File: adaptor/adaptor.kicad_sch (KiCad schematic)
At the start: 2 parts, among them CN1 XT30(2+2)PB-M.G.B, CN2 XT30(2+2)PB-M.G.B

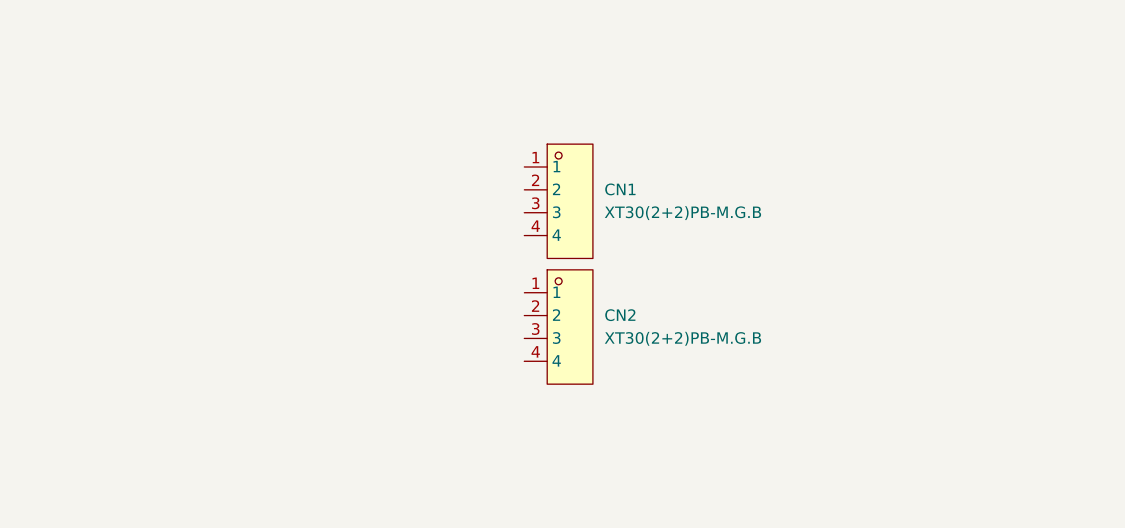
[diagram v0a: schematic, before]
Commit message: [Hw] Rough adaptor board layout, and form factor
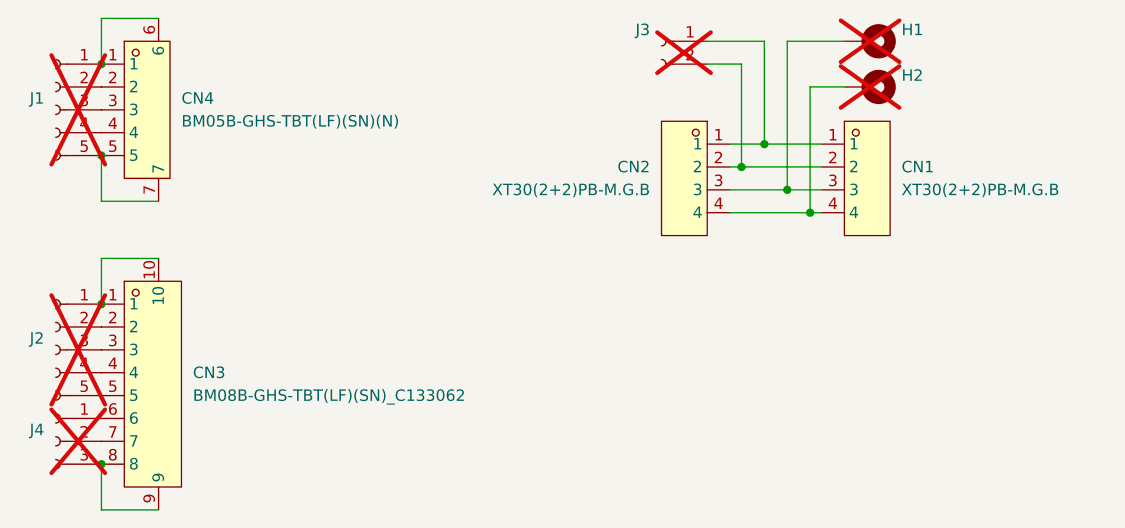
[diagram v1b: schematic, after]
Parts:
- added CN3: BM08B-GHS-TBT(LF)(SN)_C133062, easyeda:CONN-SMD_BM08B-GHS-TBT-LF-SN, symbol easyeda:BM08B-GHS-TBT(LF)(SN)_C133062
- added CN4: BM05B-GHS-TBT(LF)(SN)(N), easyeda:CONN-SMD_BM05B-GHS-TBT, symbol easyeda:BM05B-GHS-TBT(LF)(SN)(N)
- added H1, H2: ~, TestPoint:TestPoint_Keystone_5005-5009_Compact, symbol Mechanical:MountingHole_Pad
- added J1, J2: Conn_01x05_Socket, Connector_PinHeader_2.00mm:PinHeader_1x05_P2.00mm_Vertical, symbol Connector:Conn_01x05_Socket
- added J3: ~, Connector_PinHeader_2.00mm:PinHeader_1x02_P2.00mm_Vertical, symbol Connector:Conn_01x02_Socket
- added J4: Conn_01x05_Socket, Connector_PinHeader_2.00mm:PinHeader_1x03_P2.00mm_Vertical, symbol Connector:Conn_01x03_Socket
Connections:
- net at CN1.1: now also CN2.1, J3.1 (Pin_1)
- net at CN1.2: now also CN2.2, J3.2 (Pin_2)
- net at CN1.3: now also CN2.3, H1.1
- net at CN1.4: now also CN2.4, H2.1
- new net: CN3.1, CN3.10, J2.1 (Pin_1)
- new net: CN3.2, J2.2 (Pin_2)
- new net: CN3.3, J2.3 (Pin_3)
- new net: CN3.4, J2.4 (Pin_4)
- new net: CN3.5, J2.5 (Pin_5)
- new net: CN4.1, CN4.6, J1.1 (Pin_1)
- new net: CN4.2, J1.2 (Pin_2)
- new net: CN4.3, J1.3 (Pin_3)
- new net: CN4.4, J1.4 (Pin_4)
- new net: CN4.5, CN4.7, J1.5 (Pin_5)
- new net: CN3.6, J4.1 (Pin_1)
- new net: CN3.7, J4.2 (Pin_2)
- new net: CN3.8, CN3.9, J4.3 (Pin_3)
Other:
- moved on the sheet: CN1, CN2

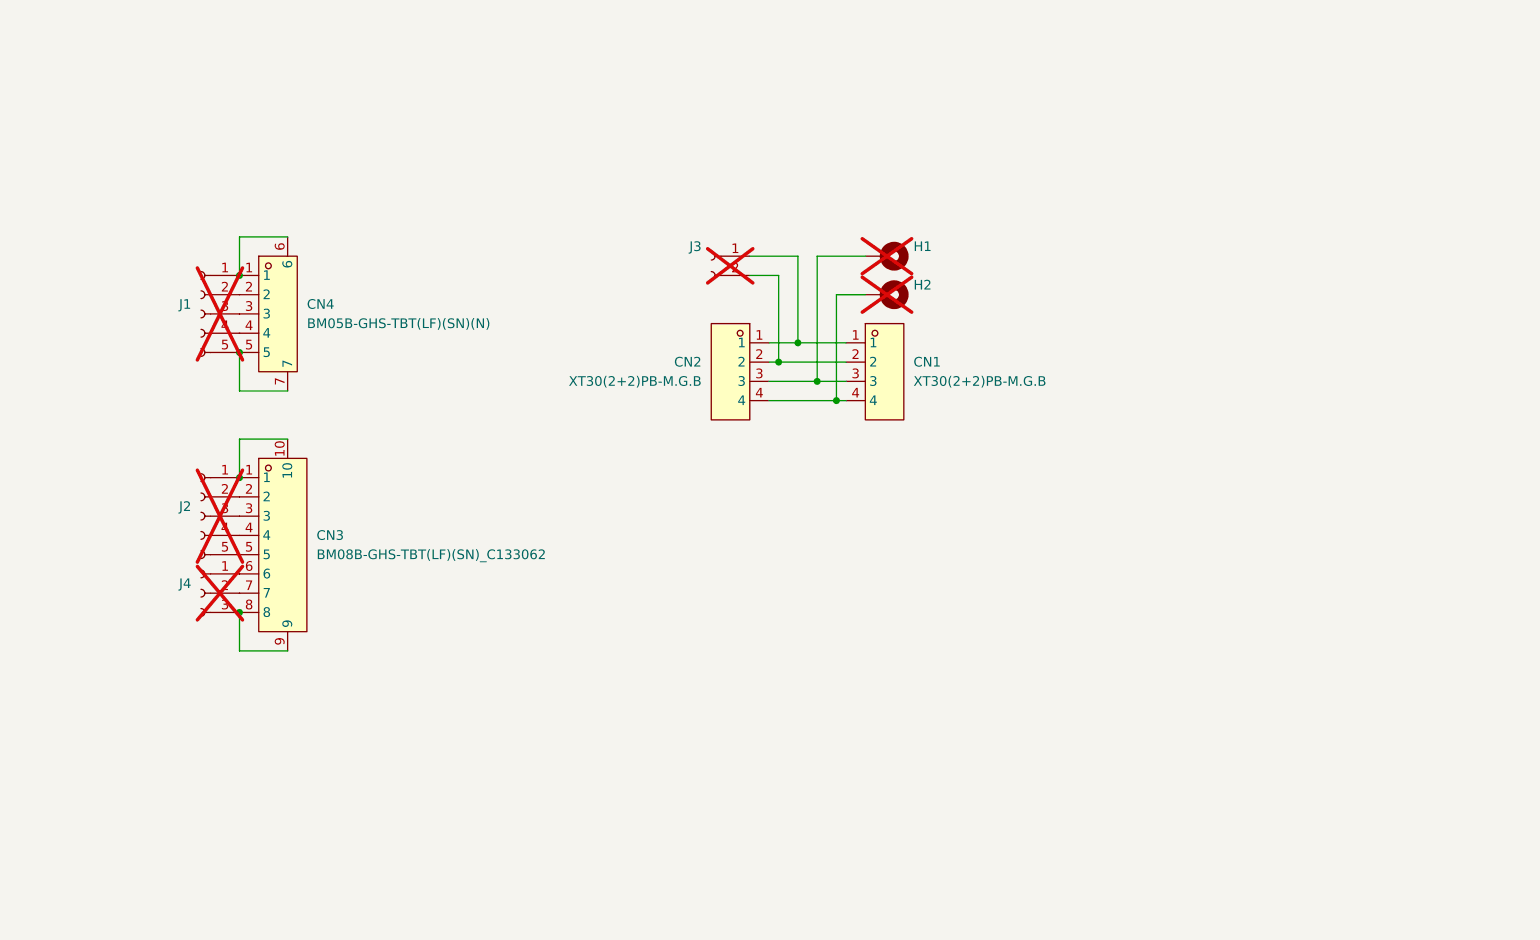
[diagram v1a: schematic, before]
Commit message: Adaptor boards
- CAN/Power XT30 2+2
- Break out Aux ports to 10 and 8 pin jst GH
- AS5046D encoder board with 10 pin jst GH connector

Signed-off-by: Will Haarhoff <williamhaarhoff@gmail.com>
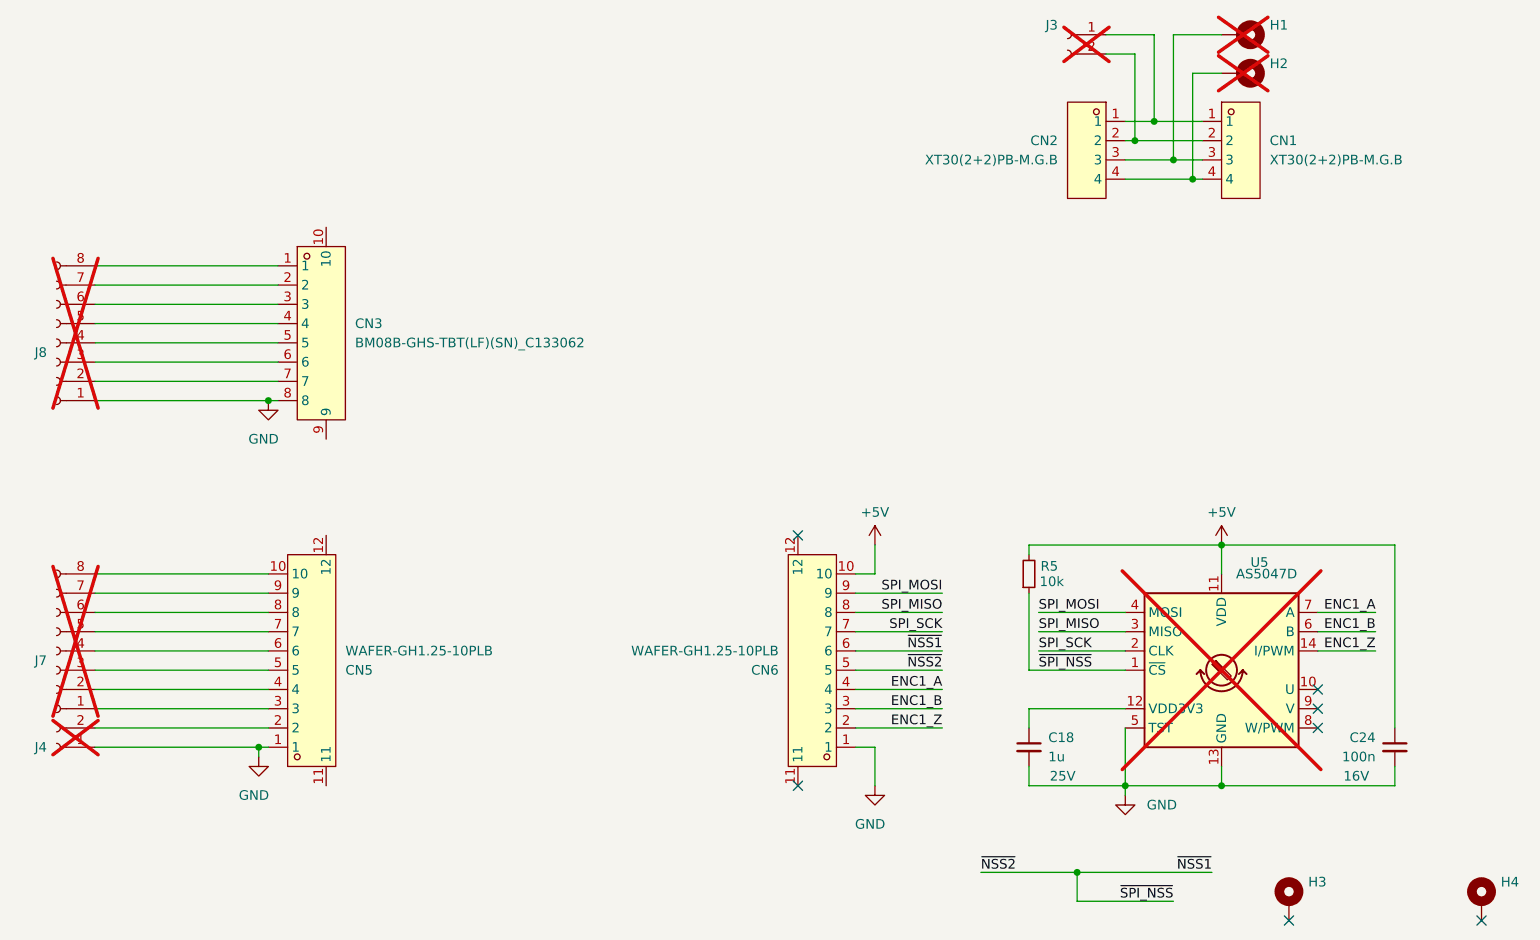
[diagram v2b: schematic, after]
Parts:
- removed CN4: BM05B-GHS-TBT(LF)(SN)(N), easyeda:CONN-SMD_BM05B-GHS-TBT, symbol easyeda:BM05B-GHS-TBT(LF)(SN)(N)
- removed J1, J2: Conn_01x05_Socket, Connector_PinHeader_2.00mm:PinHeader_1x05_P2.00mm_Vertical, symbol Connector:Conn_01x05_Socket
- removed J4: Conn_01x05_Socket, Connector_PinHeader_2.00mm:PinHeader_1x03_P2.00mm_Vertical, symbol Connector:Conn_01x03_Socket
- added C18: 1u, Capacitor_SMD:C_0402_1005Metric, symbol Device:C_Small
- added C24: 100n, Capacitor_SMD:C_0402_1005Metric, symbol Device:C_Small
- added CN5, CN6: WAFER-GH1.25-10PLB, easyeda:CONN-SMD_10P-P1.25_XUNPU_WAFER-GH1.25-10PLB, symbol easyeda:WAFER-GH1.25-10PLB
- added H3, H4: MountingHole_Pad, MountingHole:MountingHole_3.2mm_M3_ISO7380_Pad_TopBottom, symbol Mechanical:MountingHole_Pad
- added J4: Conn_01x02_Socket, Connector_PinHeader_1.27mm:PinHeader_1x02_P1.27mm_Vertical, symbol Connector:Conn_01x02_Socket
- added J7, J8: Conn_01x08_Socket, Connector_PinHeader_1.27mm:PinHeader_1x08_P1.27mm_Vertical, symbol Connector:Conn_01x08_Socket
- added R5: 10k, Resistor_SMD:R_0402_1005Metric, symbol Device:R_Small
- added U5: AS5047D, Package_SO:TSSOP-14_4.4x5mm_P0.65mm, symbol Sensor_Magnetic:AS5047D
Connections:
- net at CN3.1: now also J8.8 (Pin_8); no longer CN3.10
- net at CN3.2: now also J8.7 (Pin_7)
- net at CN3.3: now also J8.6 (Pin_6)
- net at CN3.4: now also J8.5 (Pin_5)
- net at CN3.5: now also J8.4 (Pin_4)
- net at CN3.6: now also J8.3 (Pin_3)
- net at CN3.7: now also J8.2 (Pin_2)
- net at CN3.9: no longer CN3.8
- new net: C18.1, U5.12 (VDD3V3)
- new net: CN5.3, J7.1 (Pin_1)
- new net: CN5.4, J7.2 (Pin_2)
- new net: CN5.5, J7.3 (Pin_3)
- new net: CN5.6, J7.4 (Pin_4)
- new net: CN5.7, J7.5 (Pin_5)
- new net: CN5.8, J7.6 (Pin_6)
- new net: CN5.9, J7.7 (Pin_7)
- new net: CN5.10, J7.8 (Pin_8)
- new net: CN5.2, J4.2 (Pin_2)
- new net +5V: C24.1, CN6.10, R5.2, U5.11 (VDD)
- new net ENC1_A: CN6.4, U5.7 (A)
- new net ENC1_B: CN6.3, U5.6 (B)
- new net ENC1_Z: CN6.2, U5.14 (I/PWM)
- new net GND: C18.2, C24.2, CN3.8, CN5.1, CN6.1, J4.1 (Pin_1), J8.1 (Pin_1), U5.13 (GND), U5.5 (TST)
- new net SPI_MISO: CN6.8, U5.3 (MISO)
- new net SPI_MOSI: CN6.9, U5.4 (MOSI)
- new net SPI_SCK: CN6.7, U5.2 (CLK)
- new net ~{NSS1}: CN6.5, CN6.6, R5.1, U5.1 (~{CS})
- no-connect marks 0 -> 7
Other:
- moved on the sheet: CN1, CN2, H1, H2, J3

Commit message: [Hw] Finished adaptor board, passes DRC
Signed-off-by: Will Haarhoff <williamhaarhoff@gmail.com>
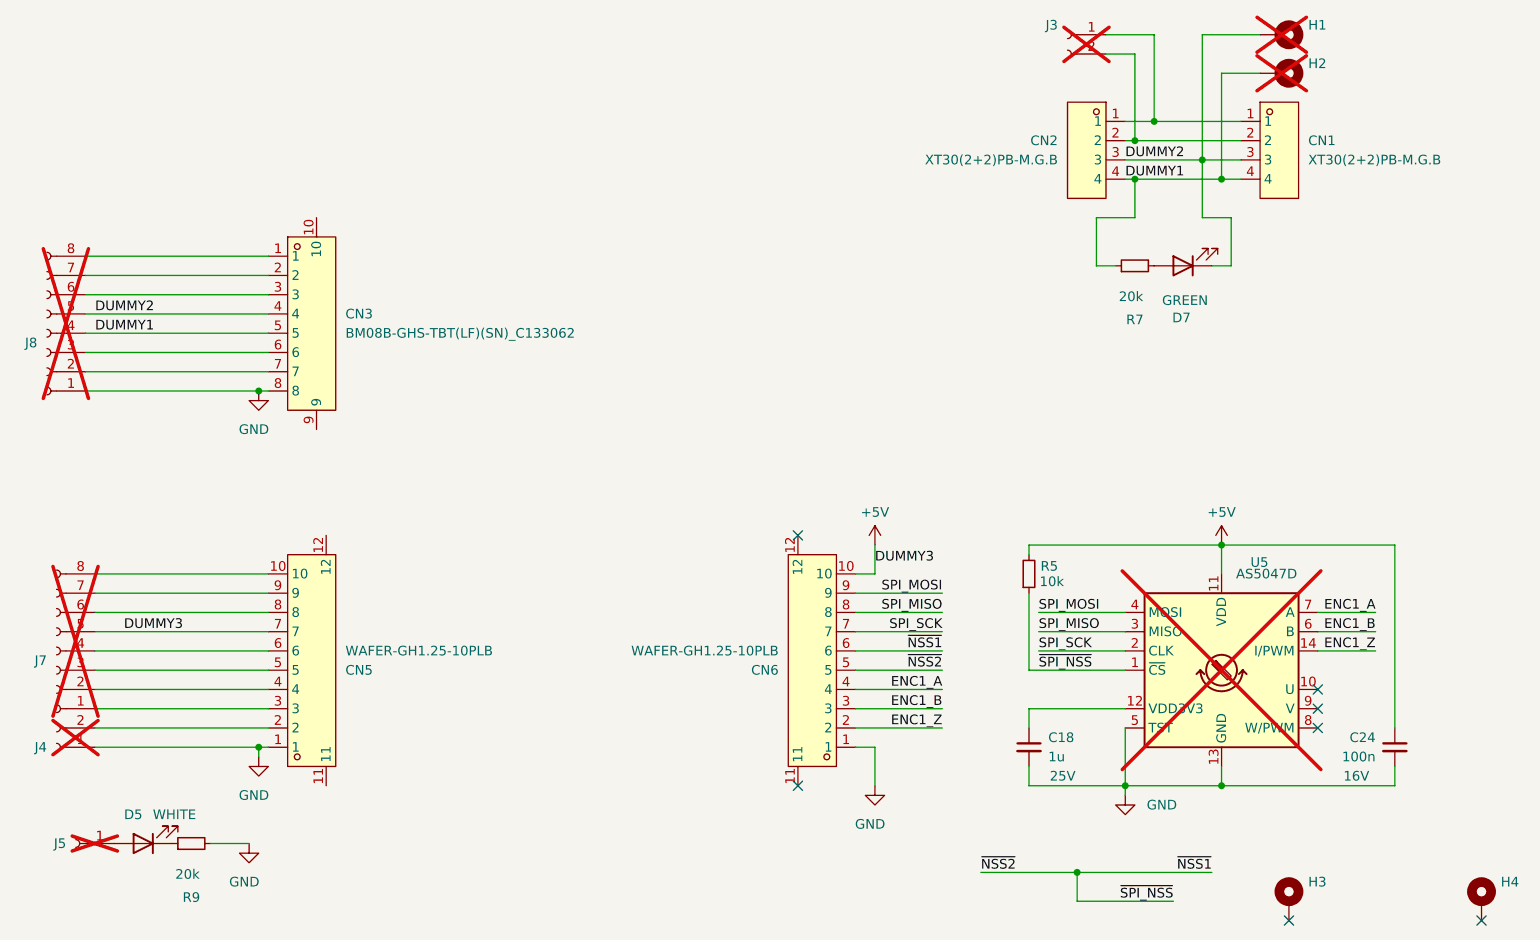
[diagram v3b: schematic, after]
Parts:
- added D5: WHITE, LED_SMD:LED_0603_1608Metric, symbol Device:LED
- added D7: GREEN, LED_SMD:LED_0603_1608Metric, symbol Device:LED
- added J5: Conn_01x02_Socket, Connector_PinHeader_1.27mm:PinHeader_1x01_P1.27mm_Vertical, symbol Connector:Conn_01x01_Socket
- added R7, R9: 20k, Resistor_SMD:R_0402_1005Metric, symbol Device:R_Small
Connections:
- net +5V: now also CN5.7, J7.5 (Pin_5)
- net GND: now also R9.2
- net DUMMY2: now reaches CN1.3, CN2.3, H1.1
- net DUMMY2: now also CN3.4, J8.5 (Pin_5), D7.1 (K)
- net DUMMY1: now reaches CN1.4, CN2.4, H2.1
- net DUMMY1: now also CN3.5, J8.4 (Pin_4), R7.1
- new net: D5.2 (A), J5.1 (Pin_1)
- new net: D5.1 (K), R9.1
- new net: D7.2 (A), R7.2
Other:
- moved on the sheet: CN1, CN3, H1, H2, J8
